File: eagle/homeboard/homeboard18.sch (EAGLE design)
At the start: 131 parts, among them IC1 XCF02S, IC2 25LC080SN, IC3 ATMEGA32U2-TQFP, Q5 BC848SMD, Q6 BC848SMD, Q7 BC848SMD, Q8 BC848SMD, T1 BSS138, T2 BC848, T3 BSS138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

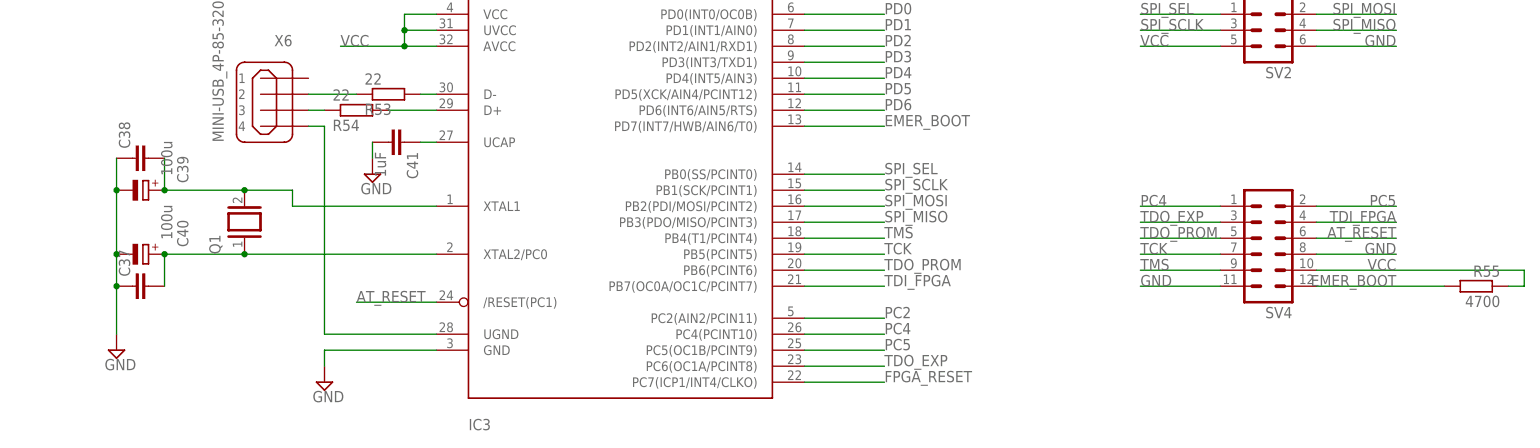
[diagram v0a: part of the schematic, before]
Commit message: pull at_reset high
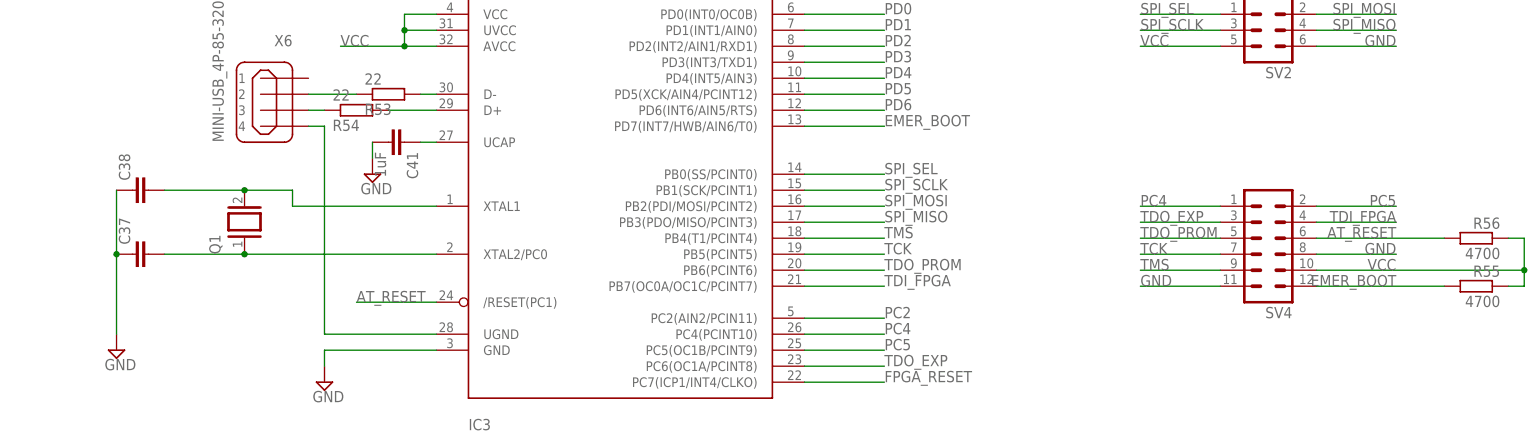
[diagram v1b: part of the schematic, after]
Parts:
- removed C39, C40: 100u, rcl:CPOL-EUD
- added R56: 4700, rcl:R-EU_R0805
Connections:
- net AT_RESET: now also R56.2
- net GND: no longer C39.-, C40.-
- net N$12: no longer C40.+
- net N$14: no longer C39.+
- net VCC: now also R56.1
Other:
- moved on the sheet: C37, C38
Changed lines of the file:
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@@
 <part name="C38" library="rcl" deviceset="C-EU" device="C0805"/>
 <part name="SUPPLY20" library="supply2" deviceset="GND" device=""/>
-<part name="C39" library="rcl" deviceset="CPOL-EU" device="D" value="100u"/>
-<part name="C40" library="rcl" deviceset="CPOL-EU" device="D" value="100u"/>
 <part name="PWR_HDR" library="jumper" deviceset="JP1Q" device=""/>
 <part name="SUPPLY21" library="supply2" deviceset="GND" device=""/>
@@
 <part name="R55" library="rcl" deviceset="R-EU_" device="R0805" value="4700"/>
 <part name="SV2" library="con-lstb" deviceset="MA03-2" device=""/>
+<part name="R56" library="rcl" deviceset="R-EU_" device="R0805" value="4700"/>
 </parts>
 <sheets>
@@
 <instance part="SJ1" gate="G$1" x="378.46" y="50.8" rot="R180"/>
 <instance part="SJ2" gate="1" x="386.08" y="38.1" rot="R270"/>
-<instance part="C37" gate="G$1" x="335.28" y="91.44" rot="R90"/>
-<instance part="C38" gate="G$1" x="335.28" y="111.76" rot="R90"/>
+<instance part="C37" gate="G$1" x="335.28" y="96.52" rot="R90"/>
+<instance part="C38" gate="G$1" x="335.28" y="106.68" rot="R90"/>
 <instance part="SUPPLY20" gate="GND" x="332.74" y="81.28"/>
-<instance part="C39" gate="G$1" x="337.82" y="106.68" smashed="yes" rot="R270">
-<attribute name="NAME" x="342.3666" y="112.141" size="1.778" layer="95" rot="R270"/>
-<attribute name="VALUE" x="339.8266" y="114.554" size="1.778" layer="96" rot="R270"/>
-</instance>
-<instance part="C40" gate="G$1" x="337.82" y="96.52" smashed="yes" rot="R270">
-<attribute name="NAME" x="342.3666" y="101.981" size="1.778" layer="95" rot="R270"/>
-<attribute name="VALUE" x="339.8266" y="104.394" size="1.778" layer="96" rot="R270"/>
-</instance>
 <instance part="PWR_HDR" gate="A" x="-297.18" y="50.8" rot="R90"/>
 <instance part="SUPPLY21" gate="GND" x="-289.56" y="38.1"/>
@@
 <instance part="R55" gate="G$1" x="548.64" y="91.44" rot="MR0"/>
 <instance part="SV2" gate="1" x="515.62" y="132.08" rot="R180"/>
+<instance part="R56" gate="G$1" x="548.64" y="99.06" rot="MR0"/>
 </instances>
 <busses>
@@
 <segment>
 <pinref part="C38" gate="G$1" pin="1"/>
-<pinref part="C39" gate="G$1" pin="-"/>
-<wire x1="332.74" y1="111.76" x2="332.74" y2="106.68" width="0.1524" layer="91"/>
-<pinref part="C40" gate="G$1" pin="-"/>
 <wire x1="332.74" y1="106.68" x2="332.74" y2="96.52" width="0.1524" layer="91"/>
-<junction x="332.74" y="106.68"/>
 <pinref part="C37" gate="G$1" pin="1"/>
-<wire x1="332.74" y1="96.52" x2="332.74" y2="91.44" width="0.1524" layer="91"/>
+<pinref part="SUPPLY20" gate="GND" pin="GND"/>
+<wire x1="332.74" y1="83.82" x2="332.74" y2="96.52" width="0.1524" layer="91"/>
 <junction x="332.74" y="96.52"/>
-<pinref part="SUPPLY20" gate="GND" pin="GND"/>
-<wire x1="332.74" y1="83.82" x2="332.74" y2="91.44" width="0.1524" layer="91"/>
-<junction x="332.74" y="91.44"/>
 </segment>
 <segment>
@@
 <wire x1="556.26" y1="91.44" x2="556.26" y2="93.98" width="0.1524" layer="91"/>
 <wire x1="556.26" y1="93.98" x2="523.24" y2="93.98" width="0.1524" layer="91"/>
+<pinref part="R56" gate="G$1" pin="1"/>
+<wire x1="553.72" y1="99.06" x2="556.26" y2="99.06" width="0.1524" layer="91"/>
+<wire x1="556.26" y1="99.06" x2="556.26" y2="93.98" width="0.1524" layer="91"/>
+<junction x="556.26" y="93.98"/>
 </segment>
 <segment>
@@
 <segment>
 <pinref part="C37" gate="G$1" pin="2"/>
-<pinref part="C40" gate="G$1" pin="+"/>
-<wire x1="340.36" y1="91.44" x2="340.36" y2="96.52" width="0.1524" layer="91"/>
 <pinref part="Q1" gate="G$1" pin="1"/>
 <wire x1="340.36" y1="96.52" x2="353.06" y2="96.52" width="0.1524" layer="91"/>
-<junction x="340.36" y="96.52"/>
 <pinref part="IC3" gate="G$1" pin="XTAL2/PC0"/>
 <wire x1="383.54" y1="96.52" x2="353.06" y2="96.52" width="0.1524" layer="91"/>
@@
 <segment>
 <pinref part="C38" gate="G$1" pin="2"/>
-<pinref part="C39" gate="G$1" pin="+"/>
 <pinref part="Q1" gate="G$1" pin="2"/>
 <wire x1="353.06" y1="106.68" x2="340.36" y2="106.68" width="0.1524" layer="91"/>
-<wire x1="340.36" y1="106.68" x2="340.36" y2="111.76" width="0.1524" layer="91"/>
-<junction x="340.36" y="106.68"/>
 <pinref part="IC3" gate="G$1" pin="XTAL1"/>
 <wire x1="383.54" y1="104.14" x2="360.68" y2="104.14" width="0.1524" layer="91"/>
@@
 </segment>
 <segment>
-<wire x1="535.94" y1="99.06" x2="523.24" y2="99.06" width="0.1524" layer="91"/>
+<wire x1="543.56" y1="99.06" x2="523.24" y2="99.06" width="0.1524" layer="91"/>
 <label x="535.94" y="99.06" size="1.778" layer="95" rot="MR0"/>
 <pinref part="SV4" gate="1" pin="6"/>
-</segment>
-</net>
+<pinref part="R56" gate="G$1" pin="2"/>
+</segment>
+</net>

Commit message: mah
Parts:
- added U$1: SDMMCSCDA, adafruit:SDMMCSCDA
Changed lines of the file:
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@@
 <part name="SV2" library="con-lstb" deviceset="MA03-2" device=""/>
 <part name="R56" library="rcl" deviceset="R-EU_" device="R0805" value="4700"/>
+<part name="U$1" library="adafruit" deviceset="SDMMC" device="SCDA"/>
 </parts>
 <sheets>
@@
 <instance part="SV2" gate="1" x="515.62" y="132.08" rot="R180"/>
 <instance part="R56" gate="G$1" x="548.64" y="99.06" rot="MR0"/>
+<instance part="U$1" gate="G$1" x="492.76" y="43.18"/>
 </instances>
 <busses>

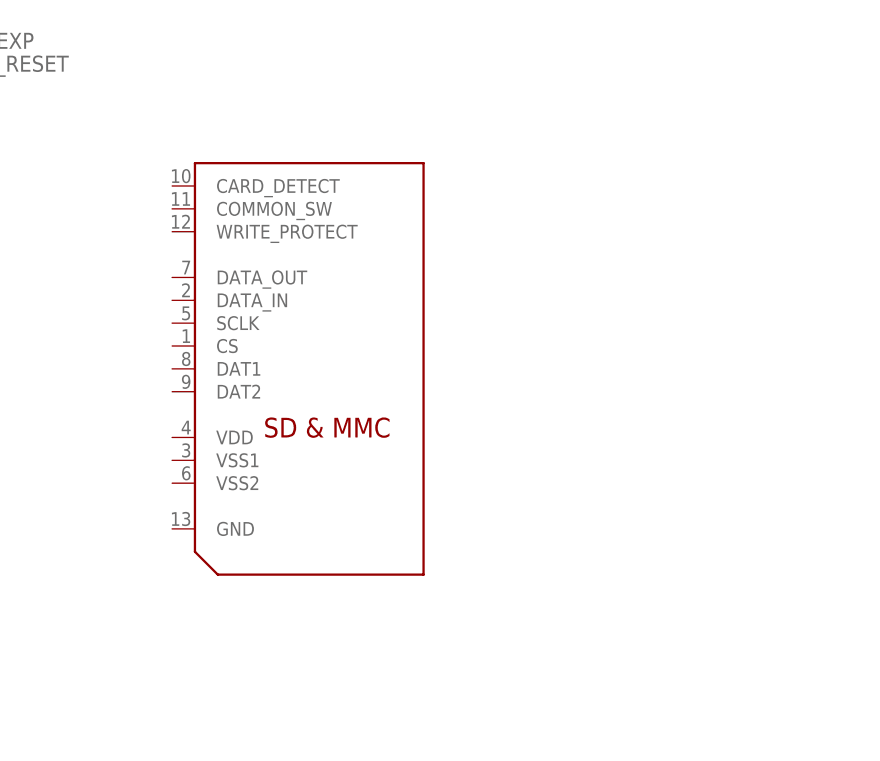
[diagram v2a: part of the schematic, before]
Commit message: sd/mmc connector to match the nohole ones i have - to mount underneatj board
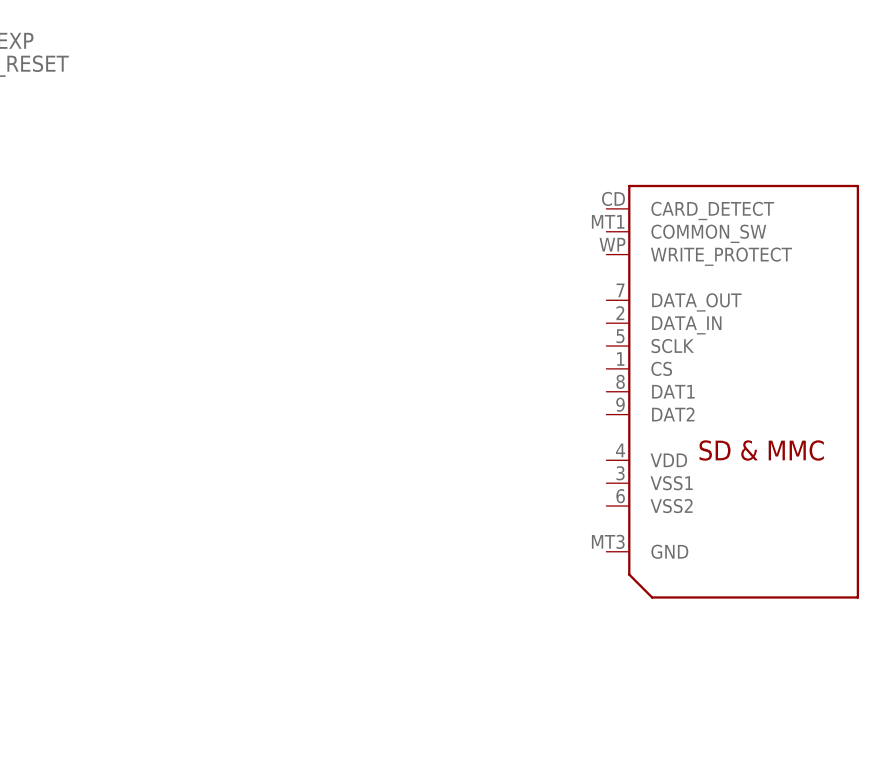
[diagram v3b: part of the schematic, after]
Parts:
- removed U$1: SDMMCSCDA, adafruit:SDMMCSCDA
- added U$3: SDMMCNOHOLE, cpcfpga:SDMMCNOHOLE
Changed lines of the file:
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@@
 <part name="SV2" library="con-lstb" deviceset="MA03-2" device=""/>
 <part name="R56" library="rcl" deviceset="R-EU_" device="R0805" value="4700"/>
-<part name="U$1" library="adafruit" deviceset="SDMMC" device="SCDA"/>
+<part name="U$3" library="cpcfpga" deviceset="SDMMC" device="NOHOLE"/>
 </parts>
 <sheets>
@@
 <instance part="SV2" gate="1" x="515.62" y="132.08" rot="R180"/>
 <instance part="R56" gate="G$1" x="548.64" y="99.06" rot="MR0"/>
-<instance part="U$1" gate="G$1" x="492.76" y="43.18"/>
+<instance part="U$3" gate="G$1" x="541.02" y="40.64"/>
 </instances>
 <busses>

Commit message: added sd/mmc connector and made a bit of a mess
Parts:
- removed C35, C36: 100u, rcl:CPOL-EUD
- added C39, C40, C42: 100u, rcl:CPOL-EUD
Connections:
- new net SD_CLK: U$3.SCLK
- new net SD_CS: U$3.CS
- new net SD_DI: U$3.DATA_IN
- new net SD_DO: U$3.DATA_OUT
- net GND: now also C39.-, C40.-, C42.-, U$3.COMMON_SW, U$3.GND, U$3.VSS1, U$3.VSS2; no longer C35.-, C36.-
- net VCC: now also C39.+, U$3.VDD
- net VCC5: no longer C35.+, C36.+
- net VCCAUX: now also C40.+
- net VCCINT: now also C42.+
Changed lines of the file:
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@@
 <part name="U$6" library="cpcfpga" deviceset="AS6C4008" device=""/>
 <part name="C34" library="rcl" deviceset="C-EU" device="C0603" value="100nF"/>
-<part name="C35" library="rcl" deviceset="CPOL-EU" device="D" value="100u"/>
-<part name="C36" library="rcl" deviceset="CPOL-EU" device="D" value="100u"/>
 <part name="JP1" library="pinhead" deviceset="PINHD-2X10" device=""/>
 <part name="SUPPLY16" library="supply2" deviceset="GND" device=""/>
@@
 <part name="R56" library="rcl" deviceset="R-EU_" device="R0805" value="4700"/>
 <part name="U$3" library="cpcfpga" deviceset="SDMMC" device="NOHOLE"/>
+<part name="C39" library="rcl" deviceset="CPOL-EU" device="D" value="100u"/>
+<part name="C40" library="rcl" deviceset="CPOL-EU" device="D" value="100u"/>
+<part name="C42" library="rcl" deviceset="CPOL-EU" device="D" value="100u"/>
+<part name="SUPPLY23" library="supply2" deviceset="GND" device=""/>
 </parts>
 <sheets>
@@
 <instance part="U$6" gate="G$1" x="45.72" y="20.32" rot="MR270"/>
 <instance part="C34" gate="G$1" x="-93.98" y="127"/>
-<instance part="C35" gate="G$1" x="-238.76" y="66.04" smashed="yes">
-<attribute name="NAME" x="-244.221" y="68.0466" size="1.778" layer="95"/>
-<attribute name="VALUE" x="-246.634" y="65.5066" size="1.778" layer="96"/>
-</instance>
-<instance part="C36" gate="G$1" x="-251.46" y="66.04" smashed="yes">
-<attribute name="NAME" x="-254.381" y="68.0466" size="1.778" layer="95"/>
-<attribute name="VALUE" x="-256.794" y="65.5066" size="1.778" layer="96"/>
-</instance>
 <instance part="JP1" gate="A" x="-5.08" y="-96.52" rot="R90"/>
 <instance part="SUPPLY16" gate="GND" x="-15.24" y="-114.3"/>
@@
 <instance part="R56" gate="G$1" x="548.64" y="99.06" rot="MR0"/>
 <instance part="U$3" gate="G$1" x="541.02" y="40.64"/>
+<instance part="C39" gate="G$1" x="-160.02" y="109.22" smashed="yes">
+<attribute name="NAME" x="-165.481" y="111.2266" size="1.778" layer="95"/>
+<attribute name="VALUE" x="-167.894" y="108.6866" size="1.778" layer="96"/>
+</instance>
+<instance part="C40" gate="G$1" x="-154.94" y="58.42" smashed="yes">
+<attribute name="NAME" x="-160.401" y="62.9666" size="1.778" layer="95"/>
+<attribute name="VALUE" x="-162.814" y="60.4266" size="1.778" layer="96"/>
+</instance>
+<instance part="C42" gate="G$1" x="-152.4" y="35.56" smashed="yes">
+<attribute name="NAME" x="-157.861" y="42.6466" size="1.778" layer="95"/>
+<attribute name="VALUE" x="-160.274" y="40.1066" size="1.778" layer="96"/>
+</instance>
+<instance part="SUPPLY23" gate="GND" x="520.7" y="15.24"/>
 </instances>
 <busses>
@@
 <wire x1="-93.98" y1="121.92" x2="-101.6" y2="121.92" width="0.1524" layer="91"/>
 <junction x="-101.6" y="121.92"/>
+<pinref part="C39" gate="G$1" pin="-"/>
+<wire x1="-160.02" y1="104.14" x2="-157.48" y2="104.14" width="0.1524" layer="91"/>
 </segment>
 <segment>
@@
 <junction x="-127" y="53.34"/>
 <pinref part="SUPPLY10" gate="GND" pin="GND"/>
+<pinref part="C40" gate="G$1" pin="-"/>
+<wire x1="-154.94" y1="53.34" x2="-149.86" y2="53.34" width="0.1524" layer="91"/>
+<junction x="-149.86" y="53.34"/>
 </segment>
 <segment>
@@
 <junction x="-127" y="30.48"/>
 <pinref part="SUPPLY11" gate="GND" pin="GND"/>
+<pinref part="C42" gate="G$1" pin="-"/>
+<wire x1="-149.86" y1="30.48" x2="-152.4" y2="30.48" width="0.1524" layer="91"/>
+<junction x="-149.86" y="30.48"/>
 </segment>
 <segment>
@@
 <pinref part="C33" gate="G$1" pin="-"/>
 <wire x1="-226.06" y1="60.96" x2="-226.06" y2="63.5" width="0.1524" layer="91"/>
-<pinref part="C36" gate="G$1" pin="-"/>
-<pinref part="C35" gate="G$1" pin="-"/>
-<wire x1="-251.46" y1="60.96" x2="-238.76" y2="60.96" width="0.1524" layer="91"/>
-<wire x1="-238.76" y1="60.96" x2="-226.06" y2="60.96" width="0.1524" layer="91"/>
-<junction x="-238.76" y="60.96"/>
-<junction x="-226.06" y="60.96"/>
 </segment>
 <segment>
@@
 <wire x1="535.94" y1="129.54" x2="523.24" y2="129.54" width="0.1524" layer="91"/>
 <label x="535.94" y="129.54" size="1.778" layer="95" rot="MR0"/>
+</segment>
+<segment>
+<pinref part="U$3" gate="G$1" pin="VSS2"/>
+<wire x1="528.32" y1="27.94" x2="520.7" y2="27.94" width="0.1524" layer="91"/>
+<wire x1="520.7" y1="27.94" x2="520.7" y2="22.86" width="0.1524" layer="91"/>
+<pinref part="U$3" gate="G$1" pin="VSS1"/>
+<wire x1="520.7" y1="22.86" x2="520.7" y2="17.78" width="0.1524" layer="91"/>
+<wire x1="528.32" y1="30.48" x2="520.7" y2="30.48" width="0.1524" layer="91"/>
+<wire x1="520.7" y1="30.48" x2="520.7" y2="27.94" width="0.1524" layer="91"/>
+<junction x="520.7" y="27.94"/>
+<pinref part="U$3" gate="G$1" pin="GND"/>
+<wire x1="528.32" y1="22.86" x2="520.7" y2="22.86" width="0.1524" layer="91"/>
+<junction x="520.7" y="22.86"/>
+<pinref part="SUPPLY23" gate="GND" pin="GND"/>
+<pinref part="U$3" gate="G$1" pin="COMMON_SW"/>
+<wire x1="528.32" y1="58.42" x2="520.7" y2="58.42" width="0.1524" layer="91"/>
+<wire x1="520.7" y1="58.42" x2="520.7" y2="30.48" width="0.1524" layer="91"/>
+<junction x="520.7" y="30.48"/>
 </segment>
 </net>
@@
 <junction x="-170.18" y="111.76"/>
 <pinref part="C7" gate="G$1" pin="1"/>
-<wire x1="-165.1" y1="111.76" x2="-147.32" y2="111.76" width="0.1524" layer="91"/>
+<wire x1="-165.1" y1="111.76" x2="-160.02" y2="111.76" width="0.1524" layer="91"/>
+<wire x1="-160.02" y1="111.76" x2="-147.32" y2="111.76" width="0.1524" layer="91"/>
 <wire x1="-147.32" y1="111.76" x2="-139.7" y2="111.76" width="0.1524" layer="91"/>
 <junction x="-147.32" y="111.76"/>
@@
 <pinref part="U$5" gate="G$1" pin="VOUT2"/>
 <pinref part="U$5" gate="G$1" pin="VOUT3"/>
+<pinref part="C39" gate="G$1" pin="+"/>
+<junction x="-160.02" y="111.76"/>
 </segment>
 <segment>
@@
 <label x="495.3" y="129.54" size="1.778" layer="95"/>
 </segment>
+<segment>
+<pinref part="U$3" gate="G$1" pin="VDD"/>
+<wire x1="510.54" y1="33.02" x2="528.32" y2="33.02" width="0.1524" layer="91"/>
+<label x="510.54" y="33.02" size="1.778" layer="95"/>
+</segment>
 </net>
 <net name="TCK" class="0">
@@
 <pinref part="REG1.2" gate="G$1" pin="VOUT1"/>
 <label x="-167.64" y="38.1" size="1.778" layer="95"/>
-<wire x1="-142.24" y1="38.1" x2="-172.72" y2="38.1" width="0.1524" layer="91"/>
+<wire x1="-142.24" y1="38.1" x2="-152.4" y2="38.1" width="0.1524" layer="91"/>
+<pinref part="C42" gate="G$1" pin="+"/>
+<wire x1="-152.4" y1="38.1" x2="-172.72" y2="38.1" width="0.1524" layer="91"/>
+<junction x="-152.4" y="38.1"/>
 </segment>
 </net>
@@
 <pinref part="REG2.5" gate="G$1" pin="VOUT1"/>
 <label x="-167.64" y="60.96" size="1.778" layer="95"/>
-<wire x1="-142.24" y1="60.96" x2="-172.72" y2="60.96" width="0.1524" layer="91"/>
+<wire x1="-142.24" y1="60.96" x2="-154.94" y2="60.96" width="0.1524" layer="91"/>
+<pinref part="C40" gate="G$1" pin="+"/>
+<wire x1="-154.94" y1="60.96" x2="-172.72" y2="60.96" width="0.1524" layer="91"/>
+<junction x="-154.94" y="60.96"/>
 </segment>
 <segment>
@@
 <junction x="-226.06" y="73.66"/>
 <pinref part="U$5" gate="G$1" pin="VCC"/>
-<pinref part="C35" gate="G$1" pin="+"/>
-<wire x1="-226.06" y1="73.66" x2="-238.76" y2="73.66" width="0.1524" layer="91"/>
-<wire x1="-238.76" y1="73.66" x2="-238.76" y2="68.58" width="0.1524" layer="91"/>
-<pinref part="C36" gate="G$1" pin="+"/>
-<wire x1="-238.76" y1="73.66" x2="-251.46" y2="73.66" width="0.1524" layer="91"/>
-<wire x1="-251.46" y1="73.66" x2="-251.46" y2="68.58" width="0.1524" layer="91"/>
-<junction x="-238.76" y="73.66"/>
 <wire x1="-226.06" y1="96.52" x2="-256.54" y2="96.52" width="0.1524" layer="91"/>
 <wire x1="-256.54" y1="96.52" x2="-264.16" y2="96.52" width="0.1524" layer="91"/>
@@
 </segment>
 </net>
+<net name="SD_CS" class="0">
+<segment>
+<pinref part="U$3" gate="G$1" pin="CS"/>
+<wire x1="510.54" y1="43.18" x2="528.32" y2="43.18" width="0.1524" layer="91"/>
+<label x="510.54" y="43.18" size="1.778" layer="95"/>
+</segment>
+</net>
+<net name="SD_CLK" class="0">
+<segment>
+<pinref part="U$3" gate="G$1" pin="SCLK"/>
+<wire x1="510.54" y1="45.72" x2="528.32" y2="45.72" width="0.1524" layer="91"/>
+<label x="510.54" y="45.72" size="1.778" layer="95"/>
+</segment>
+</net>
+<net name="SD_DI" class="0">
+<segment>
+<pinref part="U$3" gate="G$1" pin="DATA_IN"/>
+<wire x1="510.54" y1="48.26" x2="528.32" y2="48.26" width="0.1524" layer="91"/>
+<label x="510.54" y="48.26" size="1.778" layer="95"/>
+</segment>
+</net>
+<net name="SD_DO" class="0">
+<segment>
+<pinref part="U$3" gate="G$1" pin="DATA_OUT"/>
+<wire x1="510.54" y1="50.8" x2="528.32" y2="50.8" width="0.1524" layer="91"/>
+<label x="510.54" y="50.8" size="1.778" layer="95"/>
+</segment>
+</net>
